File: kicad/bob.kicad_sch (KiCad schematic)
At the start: 53 parts, among them J1 Mini USB Female, J2 GPIO (Optional), J3 GPIO (Optional), J4 Battery Connector, J5 Conn_01x03_Male, SW1 Screw Switch, U1 W25Q64JVSS, U2 AMS1117-3.3, U3 RP2040, Y1 12MHz

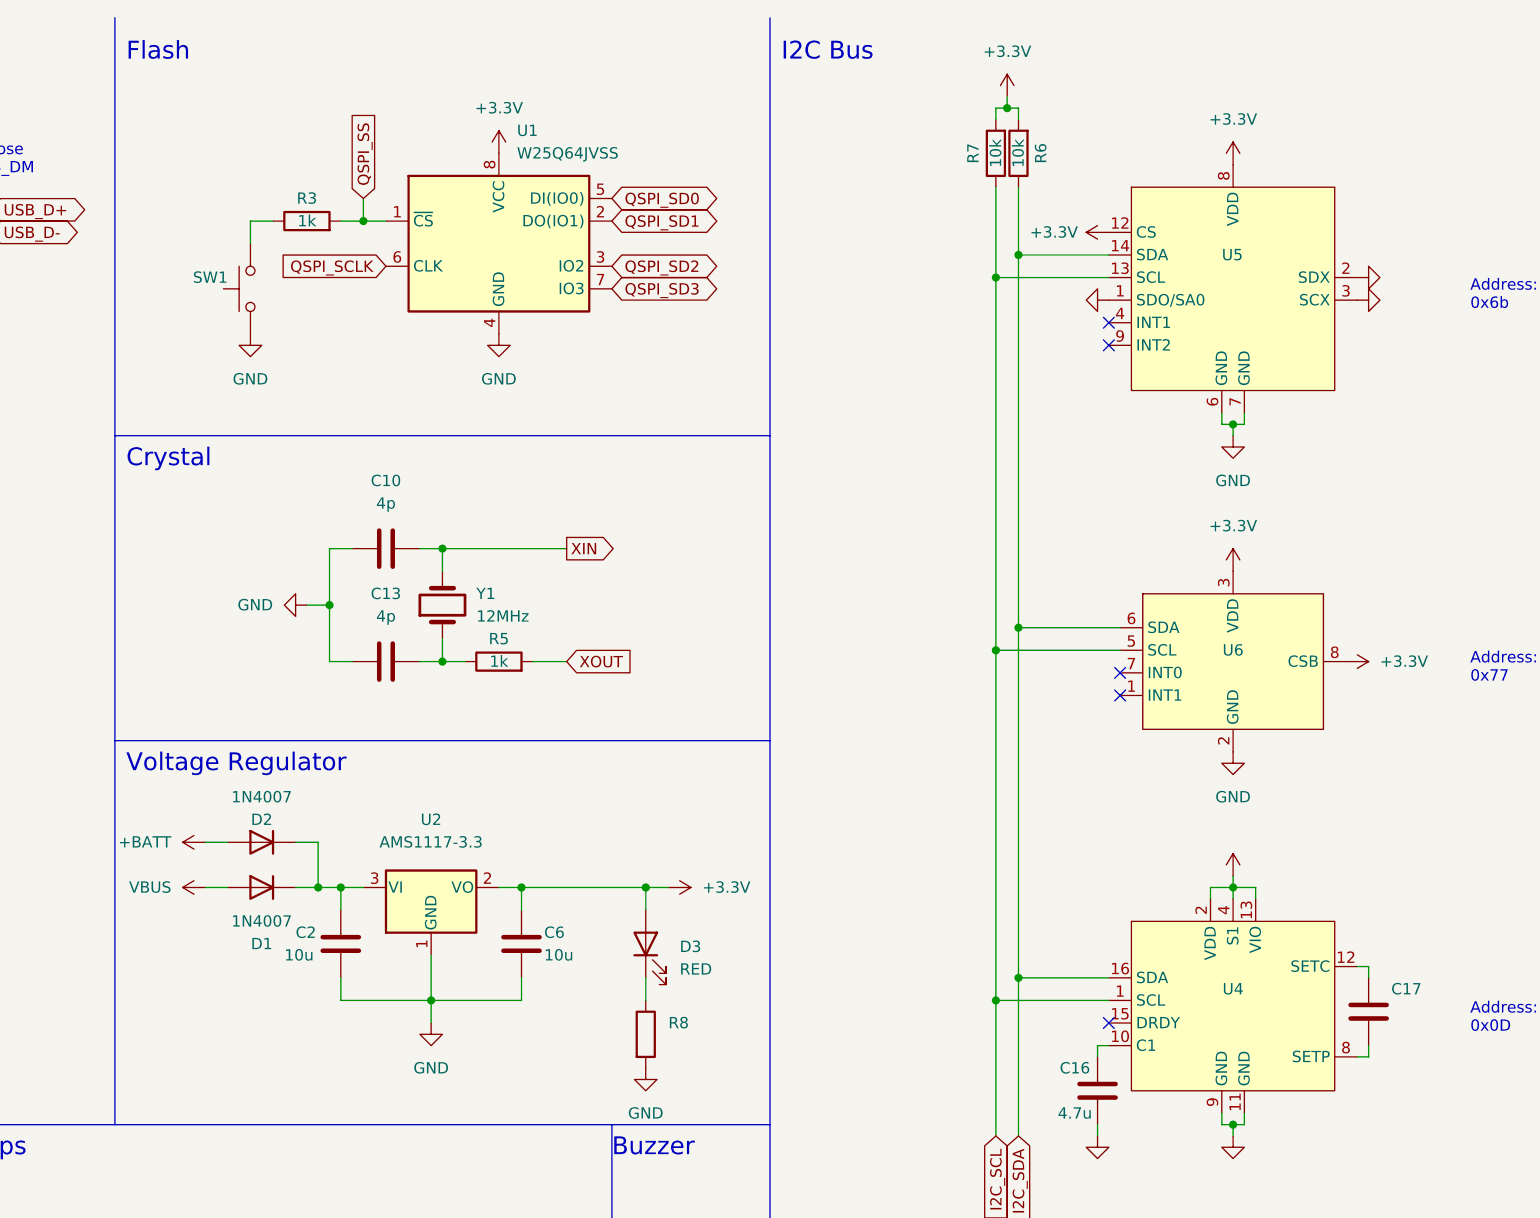
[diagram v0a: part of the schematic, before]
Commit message: Nope, switch wont fit :(
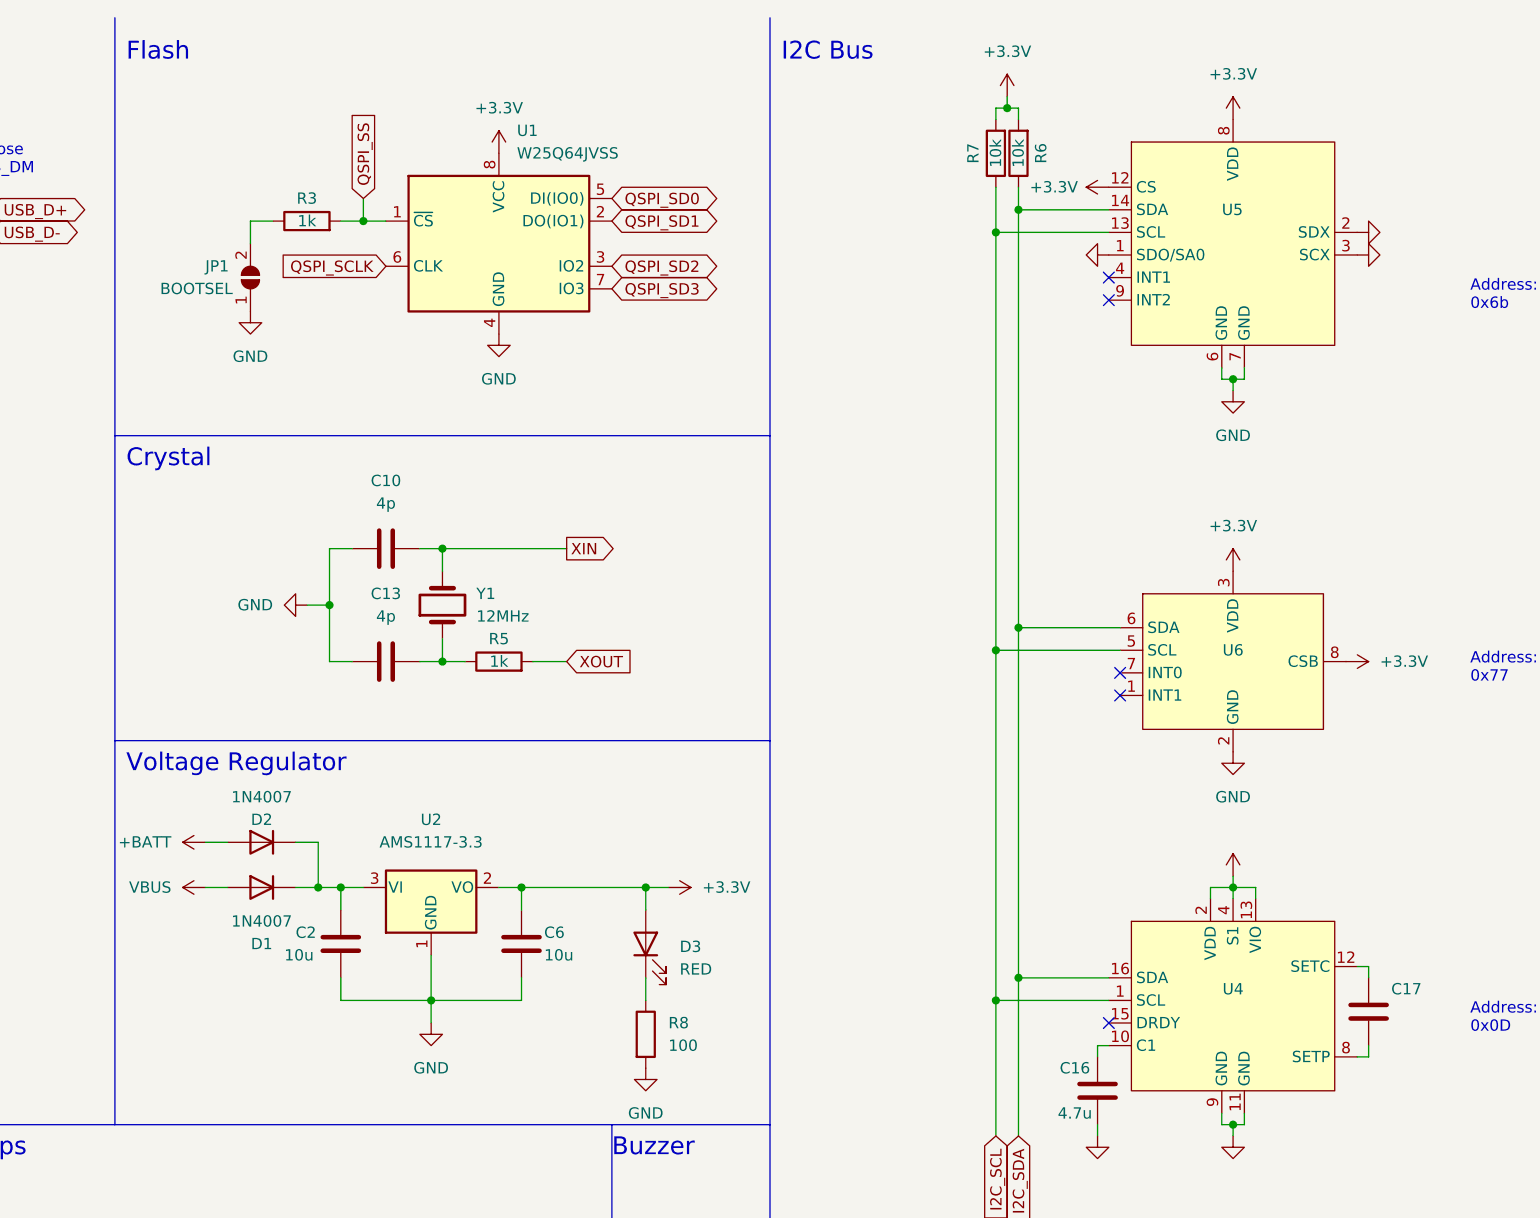
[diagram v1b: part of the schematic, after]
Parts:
- JP1: renamed from SW1; value (none) -> BOOTSEL; footprint (none) -> Jumper:SolderJumper-2_P1.3mm_Open_RoundedPad1.0x1.5mm; symbol Switch:SW_Push -> Jumper:SolderJumper_2_Open
- R8: value (none) -> 100
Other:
- moved on the sheet: U5

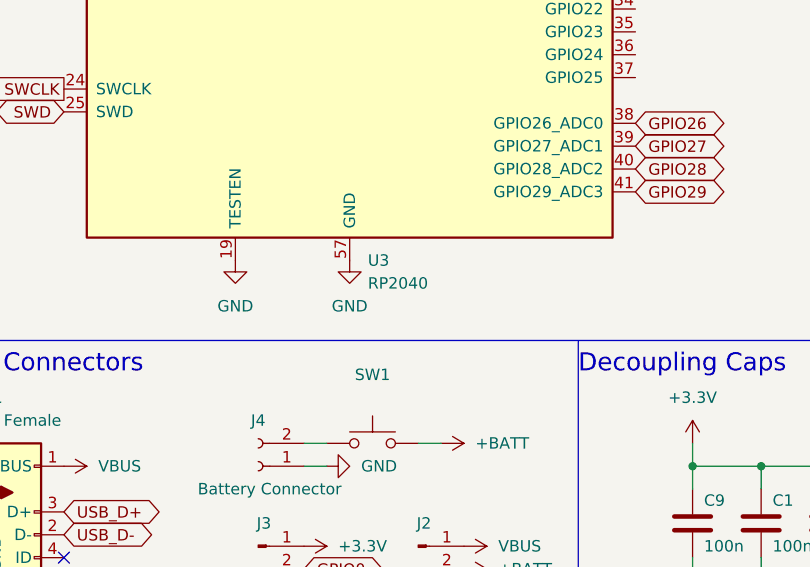
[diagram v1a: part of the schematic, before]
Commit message: Updated footprints to be much saner
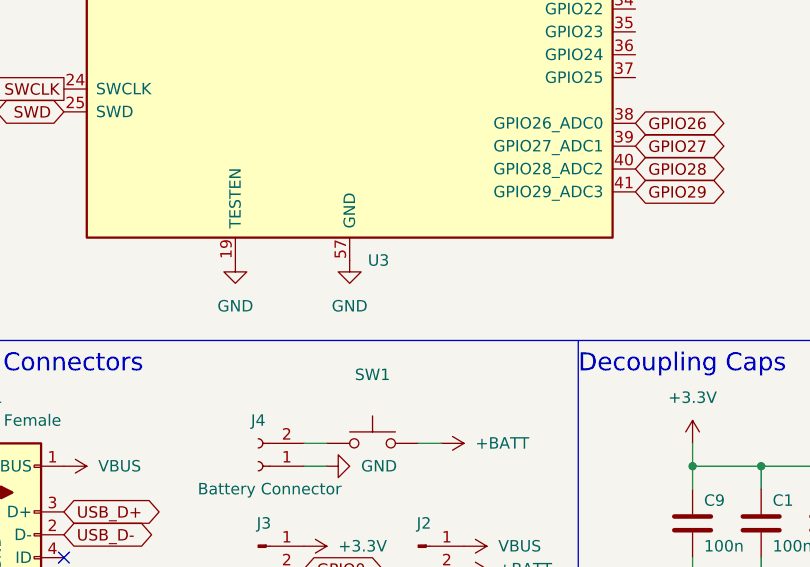
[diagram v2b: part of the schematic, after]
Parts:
- U3: value RP2040 -> (none); footprint RP2040_minimal:RP2040-QFN-56_HS -> (none)
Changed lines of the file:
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@@
   (no_connect (at 234.95 85.09))
   (no_connect (at 234.95 87.63))
-  (no_connect (at 233.68 43.18))
   (no_connect (at 233.68 40.64))
+  (no_connect (at 233.68 43.18))
   (no_connect (at 31.75 160.02))
   (wire (pts (xy 101.6 149.86) (xy 109.22 149.86))
@@
   (symbol (lib_id "power:+3.3V") (at 247.65 22.86 0) (unit 1)
     (in_bom yes) (on_board yes) (fields_autoplaced)
-    (property "Reference" "#PWR?" (id 0) (at 247.65 26.67 0)
+    (property "Reference" "#PWR0131" (id 0) (at 247.65 26.67 0)
       (effects (font (size 1.27 1.27)) hide)
     )
@@
   (symbol (lib_id "power:GND") (at 261.62 35.56 90) (unit 1)
     (in_bom yes) (on_board yes) (fields_autoplaced)
-    (property "Reference" "#PWR?" (id 0) (at 267.97 35.56 0)
+    (property "Reference" "#PWR0149" (id 0) (at 267.97 35.56 0)
       (effects (font (size 1.27 1.27)) hide)
     )
@@
   (symbol (lib_id "power:+3.3V") (at 233.68 30.48 90) (unit 1)
     (in_bom yes) (on_board yes)
-    (property "Reference" "#PWR?" (id 0) (at 237.49 30.48 0)
+    (property "Reference" "#PWR0107" (id 0) (at 237.49 30.48 0)
       (effects (font (size 1.27 1.27)) hide)
     )
@@
   (symbol (lib_id "power:GND") (at 247.65 53.34 0) (unit 1)
     (in_bom yes) (on_board yes) (fields_autoplaced)
-    (property "Reference" "#PWR?" (id 0) (at 247.65 59.69 0)
+    (property "Reference" "#PWR0106" (id 0) (at 247.65 59.69 0)
       (effects (font (size 1.27 1.27)) hide)
     )
@@
   (symbol (lib_id "power:GND") (at 233.68 38.1 270) (unit 1)
     (in_bom yes) (on_board yes) (fields_autoplaced)
-    (property "Reference" "#PWR?" (id 0) (at 227.33 38.1 0)
+    (property "Reference" "#PWR0129" (id 0) (at 227.33 38.1 0)
       (effects (font (size 1.27 1.27)) hide)
     )
@@
   (symbol (lib_id "power:GND") (at 261.62 38.1 90) (unit 1)
     (in_bom yes) (on_board yes) (fields_autoplaced)
-    (property "Reference" "#PWR?" (id 0) (at 267.97 38.1 0)
+    (property "Reference" "#PWR0130" (id 0) (at 267.97 38.1 0)
       (effects (font (size 1.27 1.27)) hide)
     )
@@
       (effects (font (size 1.27 1.27)) (justify left))
     )
-    (property "Value" "RP2040" (id 1) (at 65.5194 129.54 0)
+    (property "Value" "" (id 1) (at 65.5194 129.54 0)
       (effects (font (size 1.27 1.27)) (justify left))
     )
-    (property "Footprint" "RP2040_minimal:RP2040-QFN-56_HS" (id 2) (at 44.45 76.2 0)
+    (property "Footprint" "" (id 2) (at 44.45 76.2 0)
       (effects (font (size 1.27 1.27)) hide)
     )
@@
       (reference "#PWR0105") (unit 1) (value "GND") (footprint "")
     )
+    (path "/98a83e37-2266-4070-aae2-b4e3c95041c0"
+      (reference "#PWR0106") (unit 1) (value "GND") (footprint "")
+    )
+    (path "/8ff25ca3-7a6f-4ba9-9951-03e37d1c76eb"
+      (reference "#PWR0107") (unit 1) (value "+3.3V") (footprint "")
+    )
     (path "/0029820e-80b7-4df3-ad7f-de6b7dce0bb1"
       (reference "#PWR0108") (unit 1) (value "GND") (footprint "")
@@
       (reference "#PWR0128") (unit 1) (value "+3.3V") (footprint "")
     )
+    (path "/adbdbf00-e19f-45aa-8793-9f170a1fa9e8"
+      (reference "#PWR0129") (unit 1) (value "GND") (footprint "")
+    )
+    (path "/f9ad9c73-d652-47d9-bade-657d8c1e1da7"
+      (reference "#PWR0130") (unit 1) (value "GND") (footprint "")
+    )
+    (path "/22a21ef5-8d73-45f5-8c64-6674e766031d"
+      (reference "#PWR0131") (unit 1) (value "+3.3V") (footprint "")
+    )
     (path "/81abba7b-65ef-4439-960f-9f1a27841048"
       (reference "#PWR0132") (unit 1) (value "GND") (footprint "")
@@
       (reference "#PWR0148") (unit 1) (value "GND") (footprint "")
     )
-    (path "/22a21ef5-8d73-45f5-8c64-6674e766031d"
-      (reference "#PWR?") (unit 1) (value "+3.3V") (footprint "")
-    )
     (path "/3868f898-270d-4a4f-a12d-011ac69fd79d"
-      (reference "#PWR?") (unit 1) (value "GND") (footprint "")
-    )
-    (path "/8ff25ca3-7a6f-4ba9-9951-03e37d1c76eb"
-      (reference "#PWR?") (unit 1) (value "+3.3V") (footprint "")
-    )
-    (path "/98a83e37-2266-4070-aae2-b4e3c95041c0"
-      (reference "#PWR?") (unit 1) (value "GND") (footprint "")
-    )
-    (path "/adbdbf00-e19f-45aa-8793-9f170a1fa9e8"
-      (reference "#PWR?") (unit 1) (value "GND") (footprint "")
-    )
-    (path "/f9ad9c73-d652-47d9-bade-657d8c1e1da7"
-      (reference "#PWR?") (unit 1) (value "GND") (footprint "")
+      (reference "#PWR0149") (unit 1) (value "GND") (footprint "")
     )
     (path "/e65ef186-5520-4142-8b10-d2898e4cdc2f"
@@
     )
     (path "/fd06c2e8-ae40-46c0-9b3f-a158ea16c0a1"
-      (reference "U3") (unit 1) (value "RP2040") (footprint "RP2040_minimal:RP2040-QFN-56_HS")
+      (reference "U3") (unit 1) (value "RP2040") (footprint "YAR_MCU:RP2040-QFN-56_HS")
     )
     (path "/f22d81fd-d012-48c9-83d0-2ee9a7253ca3"
-      (reference "U4") (unit 1) (value "QMC5883L") (footprint "Silicon-Custom:LGA-16-3X3")
+      (reference "U4") (unit 1) (value "QMC5883L") (footprint "YAR_Sensors:QMC5883L-LGA16")
     )
     (path "/8b211e9a-adc6-4d52-ba4f-b814770f3d50"
-      (reference "U5") (unit 1) (value "QMI8658C") (footprint "Silicon-Custom:14LGA_2.5x3.0")
+      (reference "U5") (unit 1) (value "QMI8658C") (footprint "YAR_Sensors:QMI8658C-LGA14")
     )
     (path "/d1910422-7ae9-42c3-aa16-3778d69d2211"
-      (reference "U6") (unit 1) (value "HP203B") (footprint "RP2040_minimal:LGA-8_3.6x3.8x0.9P")
+      (reference "U6") (unit 1) (value "HP203B") (footprint "YAR_Sensors:HP203B-LGA8")
     )
     (path "/e9d165af-abdf-49f9-beea-a51c27a6ec26"

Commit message: Changed U3 to the new symbol libs
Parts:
- U3: footprint (none) -> YAR_MCU:RP2040-QFN-56_HS; symbol MCU_RaspberryPi_RP2040:RP2040 -> YAR_MCU:RP2040
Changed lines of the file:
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@@
     (pin "1")
   )
-  (symbol (lib_id "MCU_RaspberryPi_RP2040:RP2040") (at 63.5 76.2 0) (unit 1)
+  (symbol (lib_id "YAR_MCU:RP2040") (at 63.5 76.2 0) (unit 1)
     (in_bom yes) (on_board yes) (fields_autoplaced)
     (property "Reference" "U3" (id 0) (at 65.5194 127 0)
@@
       (effects (font (size 1.27 1.27)) (justify left))
     )
-    (property "Footprint" "" (id 2) (at 44.45 76.2 0)
+    (property "Footprint" "YAR_MCU:RP2040-QFN-56_HS" (id 2) (at 44.45 76.2 0)
       (effects (font (size 1.27 1.27)) hide)
     )
